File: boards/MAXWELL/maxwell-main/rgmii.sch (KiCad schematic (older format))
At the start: 54 parts, among them J11 BEL_FUSE_0826-1G1T-23-F, U2 XC7K160T-2FFG676C, U35 KSZ9031RN, U39 AT24MAC402-UDFN

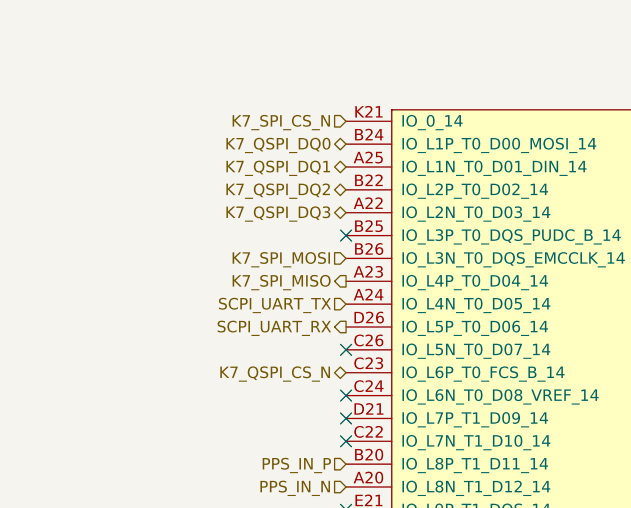
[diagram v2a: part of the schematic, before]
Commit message: Added missing PUDC_B pullup resistors
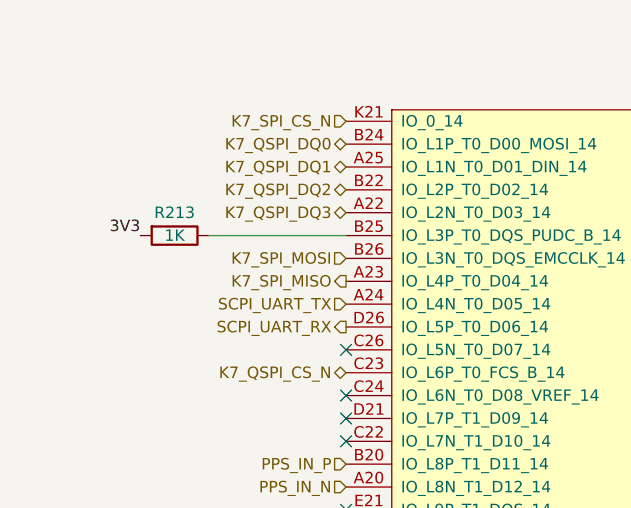
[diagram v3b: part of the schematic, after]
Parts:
- added R213: 1K, symbol device:R
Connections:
- net 3V3: now also R213.2
- net at U2.B25 (IO_L3P_T0_DQS_PUDC_B_14): now also R213.1
- no-connect marks 20 -> 19
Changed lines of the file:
@@
 Sheet 14 18
 Title "MAXWELL Main Board"
-Date "2020-06-21"
+Date "2020-06-22"
 Rev "0.1"
 Comp "Antikernel Labs"
@@
 Text Label 2050 5000 2    50   ~ 0
 MAC_I2C_SDA
-NoConn ~ 2050 1500
 NoConn ~ 2050 2000
 NoConn ~ 2050 2200
@@
 NoConn ~ 2050 2700
 NoConn ~ 2050 2800
+$Comp
+L device:R R213
+U 1 1 61DFD9AC
+P 1300 1500
+F 0 "R213" V 1200 1500 50  0000 C CNN
+F 1 "1K" V 1300 1500 50  0000 C CNN
+F 2 "" V 1230 1500 50  0001 C CNN
+F 3 "" H 1300 1500 50  0001 C CNN
+	1    1300 1500
+	0    1    1    0
+$EndComp
+Wire Wire Line
+	1450 1500 2050 1500
+Text Label 1150 1500 2    50   ~ 0
+3V3
 $EndSCHEMATC

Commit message: Continued schematic review. Added footprints for C1-C282.
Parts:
- C113, C114, C115, C120, C121, C122, C123: footprint (none) -> azonenberg_pcb:EIA_0603_CAP_NOSILK
- C116, C117, C118, C119, C124, C125, C126, C127, C128, C129, C130, C131, C132, C133, C134, C135, C136: footprint (none) -> azonenberg_pcb:EIA_0402_CAP_NOSILK
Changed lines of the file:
@@
 F 0 "U35" H 5975 7437 60  0000 C CNN
 F 1 "KSZ9031RN" H 5975 7331 60  0000 C CNN
-F 2 "" H 5150 4100 60  0000 C CNN
+F 2 "" H 5150 4100 60  0001 C CNN
 F 3 "" H 5150 4100 60  0000 C CNN
 	1    5150 4100
@@
 F 0 "J11" H 9750 3650 60  0000 L CNN
 F 1 "BEL_FUSE_0826-1G1T-23-F" H 9750 3750 60  0000 L CNN
-F 2 "" H 9750 3950 60  0000 C CNN
+F 2 "" H 9750 3950 60  0001 C CNN
 F 3 "" H 9750 3950 60  0000 C CNN
 	1    9750 3950
@@
 F 0 "C113" H 5265 4596 50  0000 L CNN
 F 1 "4.7 uF" H 5265 4505 50  0000 L CNN
-F 2 "" H 5188 4400 50  0001 C CNN
+F 2 "azonenberg_pcb:EIA_0603_CAP_NOSILK" H 5188 4400 50  0001 C CNN
 F 3 "" H 5150 4550 50  0001 C CNN
 	1    5150 4550
@@
 F 0 "FB1" V 5492 4400 40  0000 C CNN
 F 1 "600R @ 100 MHz" V 5568 4400 40  0000 C CNN
-F 2 "" H 5650 4400 60  0000 C CNN
+F 2 "" H 5650 4400 60  0001 C CNN
 F 3 "" H 5650 4400 60  0000 C CNN
 	1    5650 4400
@@
 F 0 "C120" H 6165 4596 50  0000 L CNN
 F 1 "4.7 uF" H 6165 4505 50  0000 L CNN
-F 2 "" H 6088 4400 50  0001 C CNN
+F 2 "azonenberg_pcb:EIA_0603_CAP_NOSILK" H 6088 4400 50  0001 C CNN
 F 3 "" H 6050 4550 50  0001 C CNN
 	1    6050 4550
@@
 F 0 "C126" H 6665 4596 50  0000 L CNN
 F 1 "0.47 uF" H 6665 4505 50  0000 L CNN
-F 2 "" H 6588 4400 50  0001 C CNN
+F 2 "azonenberg_pcb:EIA_0402_CAP_NOSILK" H 6588 4400 50  0001 C CNN
 F 3 "" H 6550 4550 50  0001 C CNN
 	1    6550 4550
@@
 F 0 "C130" H 7215 4596 50  0000 L CNN
 F 1 "0.47 uF" H 7215 4505 50  0000 L CNN
-F 2 "" H 7138 4400 50  0001 C CNN
+F 2 "azonenberg_pcb:EIA_0402_CAP_NOSILK" H 7138 4400 50  0001 C CNN
 F 3 "" H 7100 4550 50  0001 C CNN
 	1    7100 4550
@@
 F 0 "C114" H 5265 5046 50  0000 L CNN
 F 1 "4.7 uF" H 5265 4955 50  0000 L CNN
-F 2 "" H 5188 4850 50  0001 C CNN
+F 2 "azonenberg_pcb:EIA_0603_CAP_NOSILK" H 5188 4850 50  0001 C CNN
 F 3 "" H 5150 5000 50  0001 C CNN
 	1    5150 5000
@@
 F 0 "C121" H 6165 5046 50  0000 L CNN
 F 1 "4.7 uF" H 6165 4955 50  0000 L CNN
-F 2 "" H 6088 4850 50  0001 C CNN
+F 2 "azonenberg_pcb:EIA_0603_CAP_NOSILK" H 6088 4850 50  0001 C CNN
 F 3 "" H 6050 5000 50  0001 C CNN
 	1    6050 5000
@@
 F 0 "C127" H 6665 5046 50  0000 L CNN
 F 1 "0.47 uF" H 6665 4955 50  0000 L CNN
-F 2 "" H 6588 4850 50  0001 C CNN
+F 2 "azonenberg_pcb:EIA_0402_CAP_NOSILK" H 6588 4850 50  0001 C CNN
 F 3 "" H 6550 5000 50  0001 C CNN
 	1    6550 5000
@@
 F 0 "C115" H 5265 5596 50  0000 L CNN
 F 1 "4.7 uF" H 5265 5505 50  0000 L CNN
-F 2 "" H 5188 5400 50  0001 C CNN
+F 2 "azonenberg_pcb:EIA_0603_CAP_NOSILK" H 5188 5400 50  0001 C CNN
 F 3 "" H 5150 5550 50  0001 C CNN
 	1    5150 5550
@@
 F 0 "FB2" V 5492 5400 40  0000 C CNN
 F 1 "600R @ 100 MHz" V 5568 5400 40  0000 C CNN
-F 2 "" H 5650 5400 60  0000 C CNN
+F 2 "" H 5650 5400 60  0001 C CNN
 F 3 "" H 5650 5400 60  0000 C CNN
 	1    5650 5400
@@
 F 0 "C122" H 6165 5596 50  0000 L CNN
 F 1 "4.7 uF" H 6165 5505 50  0000 L CNN
-F 2 "" H 6088 5400 50  0001 C CNN
+F 2 "azonenberg_pcb:EIA_0603_CAP_NOSILK" H 6088 5400 50  0001 C CNN
 F 3 "" H 6050 5550 50  0001 C CNN
 	1    6050 5550
@@
 F 0 "C128" H 6665 5596 50  0000 L CNN
 F 1 "0.47 uF" H 6665 5505 50  0000 L CNN
-F 2 "" H 6588 5400 50  0001 C CNN
+F 2 "azonenberg_pcb:EIA_0402_CAP_NOSILK" H 6588 5400 50  0001 C CNN
 F 3 "" H 6550 5550 50  0001 C CNN
 	1    6550 5550
@@
 F 0 "C131" H 7215 5596 50  0000 L CNN
 F 1 "0.47 uF" H 7215 5505 50  0000 L CNN
-F 2 "" H 7138 5400 50  0001 C CNN
+F 2 "azonenberg_pcb:EIA_0402_CAP_NOSILK" H 7138 5400 50  0001 C CNN
 F 3 "" H 7100 5550 50  0001 C CNN
 	1    7100 5550
@@
 F 0 "FB3" V 5492 5900 40  0000 C CNN
 F 1 "600R @ 100 MHz" V 5568 5900 40  0000 C CNN
-F 2 "" H 5650 5900 60  0000 C CNN
+F 2 "" H 5650 5900 60  0001 C CNN
 F 3 "" H 5650 5900 60  0000 C CNN
 	1    5650 5900
@@
 F 0 "C123" H 6165 6096 50  0000 L CNN
 F 1 "4.7 uF" H 6165 6005 50  0000 L CNN
-F 2 "" H 6088 5900 50  0001 C CNN
+F 2 "azonenberg_pcb:EIA_0603_CAP_NOSILK" H 6088 5900 50  0001 C CNN
 F 3 "" H 6050 6050 50  0001 C CNN
 	1    6050 6050
@@
 F 0 "C129" H 6665 6096 50  0000 L CNN
 F 1 "0.47 uF" H 6665 6005 50  0000 L CNN
-F 2 "" H 6588 5900 50  0001 C CNN
+F 2 "azonenberg_pcb:EIA_0402_CAP_NOSILK" H 6588 5900 50  0001 C CNN
 F 3 "" H 6550 6050 50  0001 C CNN
 	1    6550 6050
@@
 F 0 "C116" H 7865 4596 50  0000 L CNN
 F 1 "0.47 uF" H 7865 4505 50  0000 L CNN
-F 2 "" H 7788 4400 50  0001 C CNN
+F 2 "azonenberg_pcb:EIA_0402_CAP_NOSILK" H 7788 4400 50  0001 C CNN
 F 3 "" H 7750 4550 50  0001 C CNN
 	1    7750 4550
@@
 F 0 "C118" H 8415 4596 50  0000 L CNN
 F 1 "0.47 uF" H 8415 4505 50  0000 L CNN
-F 2 "" H 8338 4400 50  0001 C CNN
+F 2 "azonenberg_pcb:EIA_0402_CAP_NOSILK" H 8338 4400 50  0001 C CNN
 F 3 "" H 8300 4550 50  0001 C CNN
 	1    8300 4550
@@
 F 0 "C124" H 8965 4596 50  0000 L CNN
 F 1 "0.47 uF" H 8965 4505 50  0000 L CNN
-F 2 "" H 8888 4400 50  0001 C CNN
+F 2 "azonenberg_pcb:EIA_0402_CAP_NOSILK" H 8888 4400 50  0001 C CNN
 F 3 "" H 8850 4550 50  0001 C CNN
 	1    8850 4550
@@
 F 0 "C117" H 7865 5096 50  0000 L CNN
 F 1 "0.47 uF" H 7865 5005 50  0000 L CNN
-F 2 "" H 7788 4900 50  0001 C CNN
+F 2 "azonenberg_pcb:EIA_0402_CAP_NOSILK" H 7788 4900 50  0001 C CNN
 F 3 "" H 7750 5050 50  0001 C CNN
 	1    7750 5050
@@
 F 0 "C119" H 8415 5096 50  0000 L CNN
 F 1 "0.47 uF" H 8415 5005 50  0000 L CNN
-F 2 "" H 8338 4900 50  0001 C CNN
+F 2 "azonenberg_pcb:EIA_0402_CAP_NOSILK" H 8338 4900 50  0001 C CNN
 F 3 "" H 8300 5050 50  0001 C CNN
 	1    8300 5050
@@
 F 0 "C125" H 8965 5096 50  0000 L CNN
 F 1 "0.47 uF" H 8965 5005 50  0000 L CNN
-F 2 "" H 8888 4900 50  0001 C CNN
+F 2 "azonenberg_pcb:EIA_0402_CAP_NOSILK" H 8888 4900 50  0001 C CNN
 F 3 "" H 8850 5050 50  0001 C CNN
 	1    8850 5050
@@
 F 0 "C134" V 9998 5100 50  0000 C CNN
 F 1 "0.1 uF" V 10089 5100 50  0000 C CNN
-F 2 "" H 10288 4950 50  0001 C CNN
+F 2 "azonenberg_pcb:EIA_0402_CAP_NOSILK" H 10288 4950 50  0001 C CNN
 F 3 "" H 10250 5100 50  0001 C CNN
 	1    10250 5100
@@
 F 0 "C133" V 9998 4650 50  0000 C CNN
 F 1 "0.1 uF" V 10089 4650 50  0000 C CNN
-F 2 "" H 10288 4500 50  0001 C CNN
+F 2 "azonenberg_pcb:EIA_0402_CAP_NOSILK" H 10288 4500 50  0001 C CNN
 F 3 "" H 10250 4650 50  0001 C CNN
 	1    10250 4650
@@
 F 0 "C135" V 9998 5500 50  0000 C CNN
 F 1 "0.1 uF" V 10089 5500 50  0000 C CNN
-F 2 "" H 10288 5350 50  0001 C CNN
+F 2 "azonenberg_pcb:EIA_0402_CAP_NOSILK" H 10288 5350 50  0001 C CNN
 F 3 "" H 10250 5500 50  0001 C CNN
 	1    10250 5500
@@
 F 0 "C136" V 9998 5900 50  0000 C CNN
 F 1 "0.1 uF" V 10089 5900 50  0000 C CNN
-F 2 "" H 10288 5750 50  0001 C CNN
+F 2 "azonenberg_pcb:EIA_0402_CAP_NOSILK" H 10288 5750 50  0001 C CNN
 F 3 "" H 10250 5900 50  0001 C CNN
 	1    10250 5900
@@
 F 0 "U39" H 4500 8047 60  0000 C CNN
 F 1 "AT24MAC402-UDFN" H 4500 7941 60  0000 C CNN
-F 2 "" H 4500 7550 60  0000 C CNN
+F 2 "" H 4500 7550 60  0001 C CNN
 F 3 "" H 4500 7550 60  0000 C CNN
 	1    4100 7250
@@
 F 0 "C132" H 3415 6896 50  0000 L CNN
 F 1 "0.47 uF" H 3415 6805 50  0000 L CNN
-F 2 "" H 3338 6700 50  0001 C CNN
+F 2 "azonenberg_pcb:EIA_0402_CAP_NOSILK" H 3338 6700 50  0001 C CNN
 F 3 "" H 3300 6850 50  0001 C CNN
 	1    3300 6850

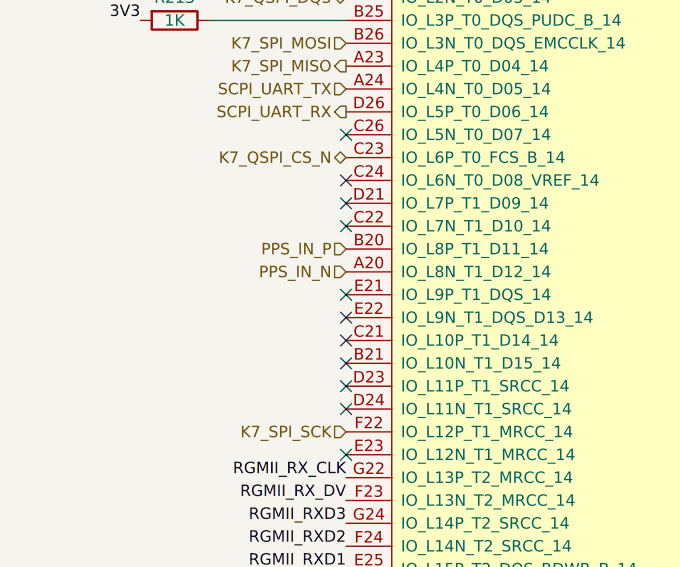
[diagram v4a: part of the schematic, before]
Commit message: Added RMII connections to FPGA
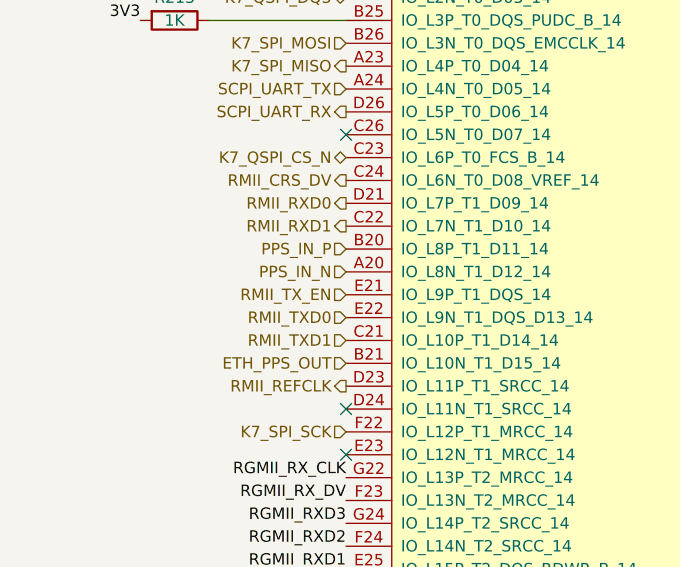
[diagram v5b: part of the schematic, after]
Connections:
- net ETH_PPS_OUT: now reaches U2.B21 (IO_L10N_T1_D15_14)
- net RMII_TXD1: now reaches U2.C21 (IO_L10P_T1_D14_14)
- net RMII_RXD1: now reaches U2.C22 (IO_L7N_T1_D10_14)
- net RMII_CRS_DV: now reaches U2.C24 (IO_L6N_T0_D08_VREF_14)
- net RMII_RXD0: now reaches U2.D21 (IO_L7P_T1_D09_14)
- net RMII_REFCLK: now reaches U2.D23 (IO_L11P_T1_SRCC_14)
- net RMII_TX_EN: now reaches U2.E21 (IO_L9P_T1_DQS_14)
- net RMII_TXD0: now reaches U2.E22 (IO_L9N_T1_DQS_D13_14)
- no-connect marks 19 -> 11
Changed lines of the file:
@@
-	1    0    0    -1
-$EndComp
-$Comp
-L xilinx-azonenberg:XC7KxT-FFG676 U?
-U 6 1 5F47F363
-P 2250 5950
-AR Path="/5EDD71F2/5F47F363" Ref="U?"  Part="9"
-AR Path="/5EF1FA37/5F47F363" Ref="U?"  Part="7"
-AR Path="/5EE2921B/5F47F363" Ref="U2"  Part="6"
-F 0 "U2" H 2250 5900 50  0000 L CNN
-F 1 "XC7K160T-2FFG676C" H 2250 5800 50  0000 L CNN
-F 2 "" H 2250 5950 50  0001 C CNN
-F 3 "" H 2250 5950 50  0001 C CNN
-	6    2250 5950
 	1    0    0    -1
 $EndComp
@@
 MAC_I2C_SDA
 NoConn ~ 2050 2000
-NoConn ~ 2050 2200
-NoConn ~ 2050 2300
 NoConn ~ 2050 5300
 NoConn ~ 2050 5200
 NoConn ~ 2050 3400
 NoConn ~ 2050 3200
-NoConn ~ 2050 3100
-NoConn ~ 2050 3000
-NoConn ~ 2050 2900
-NoConn ~ 2050 2400
 Text HLabel 2050 5900 0    50   Output ~ 0
 PLL_SYNC
@@
 Text HLabel 2050 1900 0    50   Output ~ 0
 SCPI_UART_RX
-NoConn ~ 2050 2700
-NoConn ~ 2050 2800
 $Comp
 L device:R R213
@@
 Text Label 1150 1500 2    50   ~ 0
 3V3
+Text HLabel 2050 2200 0    50   Output ~ 0
+RMII_CRS_DV
+Text HLabel 2050 2300 0    50   Output ~ 0
+RMII_RXD0
+Text HLabel 2050 2400 0    50   Output ~ 0
+RMII_RXD1
+$Comp
+L xilinx-azonenberg:XC7KxT-FFG676 U?
+U 6 1 5F47F363
+P 2250 5950
+AR Path="/5EDD71F2/5F47F363" Ref="U?"  Part="9"
+AR Path="/5EF1FA37/5F47F363" Ref="U?"  Part="7"
+AR Path="/5EE2921B/5F47F363" Ref="U2"  Part="6"
+F 0 "U2" H 2250 5900 50  0000 L CNN
+F 1 "XC7K160T-2FFG676C" H 2250 5800 50  0000 L CNN
+F 2 "" H 2250 5950 50  0001 C CNN
+F 3 "" H 2250 5950 50  0001 C CNN
+	6    2250 5950
+	1    0    0    -1
+$EndComp
+Text HLabel 2050 3100 0    50   Output ~ 0
+RMII_REFCLK
+Text HLabel 2050 2700 0    50   Input ~ 0
+RMII_TX_EN
+Text HLabel 2050 2800 0    50   Input ~ 0
+RMII_TXD0
+Text HLabel 2050 2900 0    50   Input ~ 0
+RMII_TXD1
+Text HLabel 2050 3000 0    50   Input ~ 0
+ETH_PPS_OUT
 $EndSCHEMATC

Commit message: Continued schematic review. Finished verifying pinouts. Assigned lots more footprints.
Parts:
- FB1, FB2, FB3: footprint (none) -> azonenberg_pcb:EIA_0603_INDUCTOR_NOSILK
- J11: footprint (none) -> azonenberg_pcb:CONN_BELFUSE_0826_1G1T_23_F
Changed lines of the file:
@@
 F 0 "J11" H 9750 3650 60  0000 L CNN
 F 1 "BEL_FUSE_0826-1G1T-23-F" H 9750 3750 60  0000 L CNN
-F 2 "" H 9750 3950 60  0001 C CNN
+F 2 "azonenberg_pcb:CONN_BELFUSE_0826_1G1T_23_F" H 9750 3950 60  0001 C CNN
 F 3 "" H 9750 3950 60  0000 C CNN
 	1    9750 3950
@@
 F 0 "FB1" V 5492 4400 40  0000 C CNN
 F 1 "600R @ 100 MHz" V 5568 4400 40  0000 C CNN
-F 2 "" H 5650 4400 60  0001 C CNN
+F 2 "azonenberg_pcb:EIA_0603_INDUCTOR_NOSILK" H 5650 4400 60  0001 C CNN
 F 3 "" H 5650 4400 60  0000 C CNN
 	1    5650 4400
@@
 F 0 "FB2" V 5492 5400 40  0000 C CNN
 F 1 "600R @ 100 MHz" V 5568 5400 40  0000 C CNN
-F 2 "" H 5650 5400 60  0001 C CNN
+F 2 "azonenberg_pcb:EIA_0603_INDUCTOR_NOSILK" H 5650 5400 60  0001 C CNN
 F 3 "" H 5650 5400 60  0000 C CNN
 	1    5650 5400
@@
 F 0 "FB3" V 5492 5900 40  0000 C CNN
 F 1 "600R @ 100 MHz" V 5568 5900 40  0000 C CNN
-F 2 "" H 5650 5900 60  0001 C CNN
+F 2 "azonenberg_pcb:EIA_0603_INDUCTOR_NOSILK" H 5650 5900 60  0001 C CNN
 F 3 "" H 5650 5900 60  0000 C CNN
 	1    5650 5900

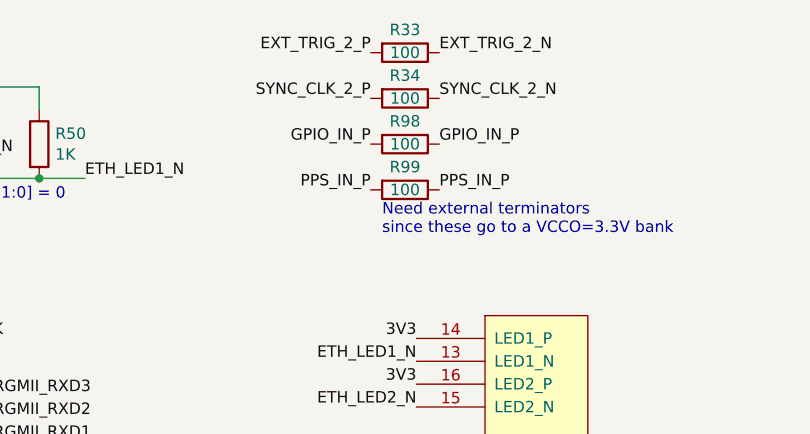
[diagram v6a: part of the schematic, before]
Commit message: Assigned footprints for all resistors
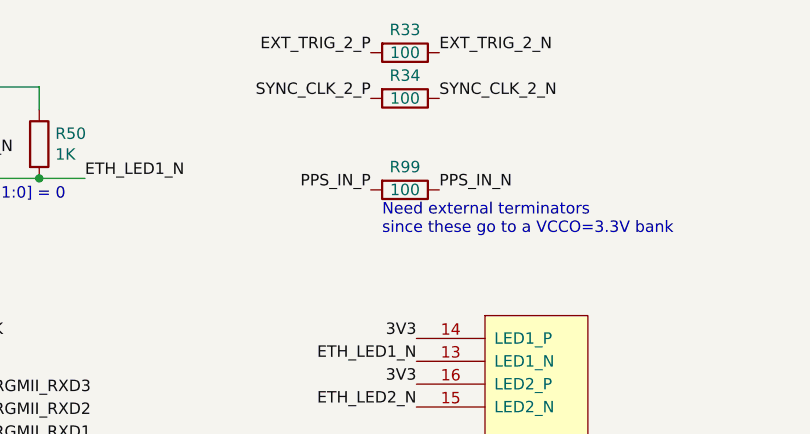
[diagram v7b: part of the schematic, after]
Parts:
- removed R98: 100, symbol device:R
- R213, R33, R34, R35, R36, R37, R38, R39, R40, R41, R42, R43, R44, R45, R46, R47, R48, R49, R50, R51, R52, R53, R99: footprint (none) -> azonenberg_pcb:EIA_0402_RES_NOSILK
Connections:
- net PPS_IN_N: now also R99.1
- net PPS_IN_P: no longer R99.1
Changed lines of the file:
@@
 Sheet 14 18
 Title "MAXWELL Main Board"
-Date "2020-06-22"
+Date "2020-06-23"
 Rev "0.1"
 Comp "Antikernel Labs"
@@
 F 0 "R33" V 9300 700 50  0000 C CNN
 F 1 "100" V 9400 700 50  0000 C CNN
-F 2 "" V 9330 700 50  0001 C CNN
+F 2 "azonenberg_pcb:EIA_0402_RES_NOSILK" V 9330 700 50  0001 C CNN
 F 3 "" H 9400 700 50  0001 C CNN
 	1    9400 700
@@
 F 0 "R34" V 9300 900 50  0000 C CNN
 F 1 "100" V 9400 900 50  0000 C CNN
-F 2 "" V 9330 900 50  0001 C CNN
+F 2 "azonenberg_pcb:EIA_0402_RES_NOSILK" V 9330 900 50  0001 C CNN
 F 3 "" H 9400 900 50  0001 C CNN
 	1    9400 900
@@
 F 0 "R41" H 7170 1046 50  0000 L CNN
 F 1 "1K" H 7170 955 50  0000 L CNN
-F 2 "" V 7030 1000 50  0001 C CNN
+F 2 "azonenberg_pcb:EIA_0402_RES_NOSILK" V 7030 1000 50  0001 C CNN
 F 3 "" H 7100 1000 50  0001 C CNN
 	1    7100 1000
@@
 F 0 "R50" H 7870 1146 50  0000 L CNN
 F 1 "1K" H 7870 1055 50  0000 L CNN
-F 2 "" V 7730 1100 50  0001 C CNN
+F 2 "azonenberg_pcb:EIA_0402_RES_NOSILK" V 7730 1100 50  0001 C CNN
 F 3 "" H 7800 1100 50  0001 C CNN
 	1    7800 1100
@@
 F 0 "R42" V 7200 2350 50  0000 C CNN
 F 1 "33" V 7250 2200 50  0000 C CNN
-F 2 "" V 7180 2200 50  0001 C CNN
+F 2 "azonenberg_pcb:EIA_0402_RES_NOSILK" V 7180 2200 50  0001 C CNN
 F 3 "" H 7250 2200 50  0001 C CNN
 	1    7250 2200
@@
 F 0 "R43" V 7200 2450 50  0000 C CNN
 F 1 "33" V 7250 2300 50  0000 C CNN
-F 2 "" V 7180 2300 50  0001 C CNN
+F 2 "azonenberg_pcb:EIA_0402_RES_NOSILK" V 7180 2300 50  0001 C CNN
 F 3 "" H 7250 2300 50  0001 C CNN
 	1    7250 2300
@@
 F 0 "R44" V 7200 2550 50  0000 C CNN
 F 1 "33" V 7250 2400 50  0000 C CNN
-F 2 "" V 7180 2400 50  0001 C CNN
+F 2 "azonenberg_pcb:EIA_0402_RES_NOSILK" V 7180 2400 50  0001 C CNN
 F 3 "" H 7250 2400 50  0001 C CNN
 	1    7250 2400
@@
 F 0 "R45" V 7200 2650 50  0000 C CNN
 F 1 "33" V 7250 2500 50  0000 C CNN
-F 2 "" V 7180 2500 50  0001 C CNN
+F 2 "azonenberg_pcb:EIA_0402_RES_NOSILK" V 7180 2500 50  0001 C CNN
 F 3 "" H 7250 2500 50  0001 C CNN
 	1    7250 2500
@@
 F 0 "R46" V 7200 2750 50  0000 C CNN
 F 1 "33" V 7250 2600 50  0000 C CNN
-F 2 "" V 7180 2600 50  0001 C CNN
+F 2 "azonenberg_pcb:EIA_0402_RES_NOSILK" V 7180 2600 50  0001 C CNN
 F 3 "" H 7250 2600 50  0001 C CNN
 	1    7250 2600
@@
 F 0 "R47" V 7200 2850 50  0000 C CNN
 F 1 "33" V 7250 2700 50  0000 C CNN
-F 2 "" V 7180 2700 50  0001 C CNN
+F 2 "azonenberg_pcb:EIA_0402_RES_NOSILK" V 7180 2700 50  0001 C CNN
 F 3 "" H 7250 2700 50  0001 C CNN
 	1    7250 2700
@@
 F 0 "R51" V 8150 3050 50  0000 C CNN
 F 1 "1K" V 8200 2900 50  0000 C CNN
-F 2 "" V 8130 2900 50  0001 C CNN
+F 2 "azonenberg_pcb:EIA_0402_RES_NOSILK" V 8130 2900 50  0001 C CNN
 F 3 "" H 8200 2900 50  0001 C CNN
 	1    8200 2900
@@
 F 0 "R48" V 7200 3250 50  0000 C CNN
 F 1 "10K" V 7250 3100 50  0000 C CNN
-F 2 "" V 7180 3100 50  0001 C CNN
+F 2 "azonenberg_pcb:EIA_0402_RES_NOSILK" V 7180 3100 50  0001 C CNN
 F 3 "" H 7250 3100 50  0001 C CNN
 	1    7250 3100
@@
 F 0 "R49" V 7200 3900 50  0000 C CNN
 F 1 "12.1K 1%" V 7350 3750 50  0000 C CNN
-F 2 "" V 7180 3750 50  0001 C CNN
+F 2 "azonenberg_pcb:EIA_0402_RES_NOSILK" V 7180 3750 50  0001 C CNN
 F 3 "" H 7250 3750 50  0001 C CNN
 	1    7250 3750
@@
 F 0 "R35" V 1350 6550 50  0000 C CNN
 F 1 "10K" V 1400 6400 50  0000 C CNN
-F 2 "" V 1330 6400 50  0001 C CNN
+F 2 "azonenberg_pcb:EIA_0402_RES_NOSILK" V 1330 6400 50  0001 C CNN
 F 3 "" H 1400 6400 50  0001 C CNN
 	1    1400 6400
@@
 F 0 "R36" V 1350 6650 50  0000 C CNN
 F 1 "10K" V 1400 6500 50  0000 C CNN
-F 2 "" V 1330 6500 50  0001 C CNN
+F 2 "azonenberg_pcb:EIA_0402_RES_NOSILK" V 1330 6500 50  0001 C CNN
 F 3 "" H 1400 6500 50  0001 C CNN
 	1    1400 6500
@@
 F 0 "R37" V 1350 6750 50  0000 C CNN
 F 1 "10K" V 1400 6600 50  0000 C CNN
-F 2 "" V 1330 6600 50  0001 C CNN
+F 2 "azonenberg_pcb:EIA_0402_RES_NOSILK" V 1330 6600 50  0001 C CNN
 F 3 "" H 1400 6600 50  0001 C CNN
 	1    1400 6600
@@
 F 0 "R38" V 1350 6850 50  0000 C CNN
 F 1 "10K" V 1400 6700 50  0000 C CNN
-F 2 "" V 1330 6700 50  0001 C CNN
+F 2 "azonenberg_pcb:EIA_0402_RES_NOSILK" V 1330 6700 50  0001 C CNN
 F 3 "" H 1400 6700 50  0001 C CNN
 	1    1400 6700
@@
 F 0 "R39" V 1350 7150 50  0000 C CNN
 F 1 "10K" V 1400 7000 50  0000 C CNN
-F 2 "" V 1330 7000 50  0001 C CNN
+F 2 "azonenberg_pcb:EIA_0402_RES_NOSILK" V 1330 7000 50  0001 C CNN
 F 3 "" H 1400 7000 50  0001 C CNN
 	1    1400 7000
@@
 F 0 "R40" V 1350 7450 50  0000 C CNN
 F 1 "10K" V 1400 7300 50  0000 C CNN
-F 2 "" V 1330 7300 50  0001 C CNN
+F 2 "azonenberg_pcb:EIA_0402_RES_NOSILK" V 1330 7300 50  0001 C CNN
 F 3 "" H 1400 7300 50  0001 C CNN
 	1    1400 7300
@@
 F 0 "R52" V 5750 6900 50  0000 C CNN
 F 1 "4.7K" V 5800 6700 50  0000 C CNN
-F 2 "" V 5730 6700 50  0001 C CNN
+F 2 "azonenberg_pcb:EIA_0402_RES_NOSILK" V 5730 6700 50  0001 C CNN
 F 3 "" H 5800 6700 50  0001 C CNN
 	1    5800 6700
@@
 F 0 "R53" V 5750 7000 50  0000 C CNN
 F 1 "4.7K" V 5800 6800 50  0000 C CNN
-F 2 "" V 5730 6800 50  0001 C CNN
+F 2 "azonenberg_pcb:EIA_0402_RES_NOSILK" V 5730 6800 50  0001 C CNN
 F 3 "" H 5800 6800 50  0001 C CNN
 	1    5800 6800
@@
 $Comp
 L device:R R?
-U 1 1 605F8A40
-P 9400 1100
-AR Path="/5EDD723A/605F8A40" Ref="R?"  Part="1"
-AR Path="/5EE2921B/605F8A40" Ref="R98"  Part="1"
-F 0 "R98" V 9300 1100 50  0000 C CNN
-F 1 "100" V 9400 1100 50  0000 C CNN
-F 2 "" V 9330 1100 50  0001 C CNN
-F 3 "" H 9400 1100 50  0001 C CNN
-	1    9400 1100
-	0    1    1    0
-$EndComp
-Text Label 9250 1100 2    50   ~ 0
-GPIO_IN_P
-Text Label 9550 1100 0    50   ~ 0
-GPIO_IN_P
-$Comp
-L device:R R?
 U 1 1 605F8A4C
 P 9400 1300
@@
 F 0 "R99" V 9300 1300 50  0000 C CNN
 F 1 "100" V 9400 1300 50  0000 C CNN
-F 2 "" V 9330 1300 50  0001 C CNN
+F 2 "azonenberg_pcb:EIA_0402_RES_NOSILK" V 9330 1300 50  0001 C CNN
 F 3 "" H 9400 1300 50  0001 C CNN
 	1    9400 1300
@@
 PPS_IN_P
 Text Label 9550 1300 0    50   ~ 0
-PPS_IN_P
+PPS_IN_N
 Text HLabel 2050 1800 0    50   Input ~ 0
 SCPI_UART_TX
@@
 F 0 "R213" V 1200 1500 50  0000 C CNN
 F 1 "1K" V 1300 1500 50  0000 C CNN
-F 2 "" V 1230 1500 50  0001 C CNN
+F 2 "azonenberg_pcb:EIA_0402_RES_NOSILK" V 1230 1500 50  0001 C CNN
 F 3 "" H 1300 1500 50  0001 C CNN
 	1    1300 1500
